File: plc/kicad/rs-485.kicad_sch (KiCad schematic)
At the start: 1 part, among them CN3 DB2ERC-5.08-4P

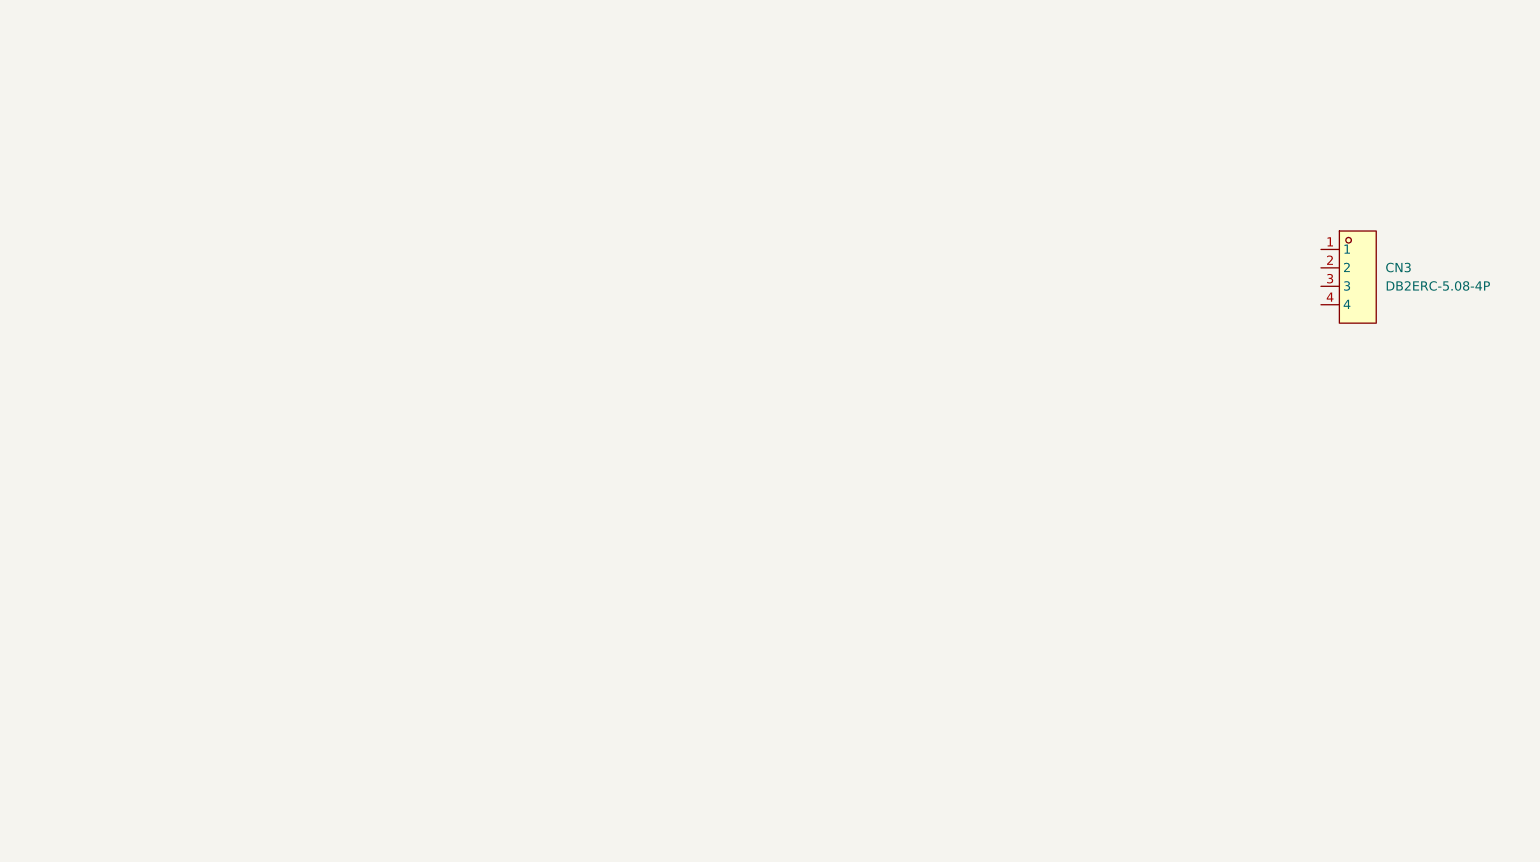
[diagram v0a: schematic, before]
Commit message: Added RS 485 circuit
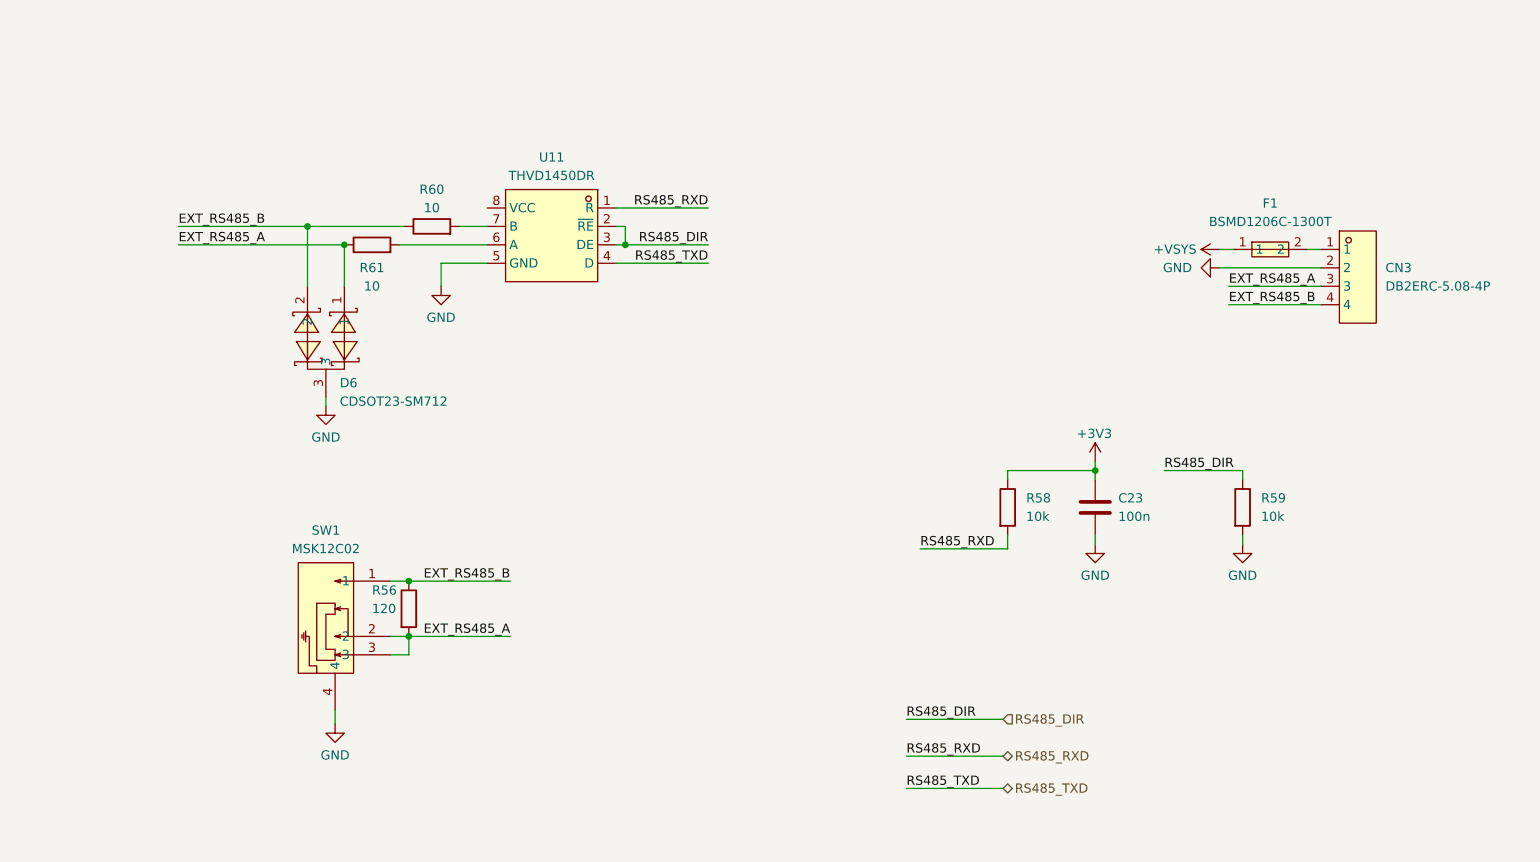
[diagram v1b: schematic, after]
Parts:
- added C23: 100n, Capacitor_SMD:C_0805_2012Metric, symbol Device:C
- added D6: CDSOT23-SM712, LibrePLC32:SOT-23_L2.9-W1.3-P1.90-LS2.4-BR, symbol LibrePLC32:CDSOT23-SM712
- added F1: BSMD1206C-1300T, LibrePLC32:F1206, symbol LibrePLC32:BSMD1206C-1300T
- added R56: 120, Resistor_SMD:R_0805_2012Metric, symbol Device:R
- added R58, R59: 10k, Resistor_SMD:R_0805_2012Metric, symbol Device:R
- added R60, R61: 10, Resistor_SMD:R_0805_2012Metric, symbol Device:R
- added SW1: MSK12C02, LibrePLC32:SW-TH_MSK12C02, symbol LibrePLC32:MSK12C02
- added U11: THVD1450DR, LibrePLC32:SOIC-8_L4.9-W3.9-P1.27-LS6.0-BL, symbol LibrePLC32:THVD1450DR
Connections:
- net at CN3.1: now also F1.2
- net GND: now reaches CN3.2
- net GND: now also C23.2, D6.3, R59.2, SW1.4, U11.5 (GND)
- net EXT_RS485_A: now reaches CN3.3
- net EXT_RS485_A: now also D6.1, R56.2, R61.1, SW1.2, SW1.3
- net EXT_RS485_B: now reaches CN3.4
- net EXT_RS485_B: now also D6.2, R56.1, R60.1, SW1.1
- new net: R60.2, U11.7 (B)
- new net: R61.2, U11.6 (A)
- new net +3V3: C23.1, R58.1
- new net +VSYS: F1.1
- new net RS485_DIR: R59.1, U11.2 (~{RE}), U11.3 (DE)
- new net RS485_RXD: R58.2, U11.1 (R)
- new net RS485_TXD: U11.4 (D)

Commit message: Added CAN circuit
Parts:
- removed F1: BSMD1206C-1300T, LibrePLC32:F1206, symbol LibrePLC32:BSMD1206C-1300T
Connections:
- net +VSYS: now also CN3.1
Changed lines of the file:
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@@
-	(wire
-		(pts
-			(xy 201.93 83.82) (xy 203.835 83.82)
-		)
-		(stroke
-			(width 0)
-			(type default)
-		)
-	)
 	(wire
 		(pts
@@
 	(wire
 		(pts
+			(xy 203.2 83.82) (xy 215.9 83.82)
+		)
+		(stroke
+			(width 0)
+			(type default)
+		)
+	)
+	(wire
+		(pts
 			(xy 203.2 91.44) (xy 215.9 91.44)
 		)
@@
 	(wire
 		(pts
-			(xy 201.93 86.36) (xy 215.9 86.36)
+			(xy 203.2 86.36) (xy 215.9 86.36)
 		)
 		(stroke
@@
 		(pts
 			(xy 58.42 80.645) (xy 76.2 80.645)
-		)
-		(stroke
-			(width 0)
-			(type default)
-		)
-	)
-	(wire
-		(pts
-			(xy 213.995 83.82) (xy 215.9 83.82)
 		)
 		(stroke
@@
 	)
 	(symbol
+		(lib_id "power:+VSW")
+		(at 203.2 83.82 90)
+		(unit 1)
+		(body_style 1)
+		(exclude_from_sim no)
+		(in_bom yes)
+		(on_board yes)
+		(in_pos_files yes)
+		(dnp no)
+		(fields_autoplaced yes)
+		(property "Reference" "#PWR0117"
+			(at 207.01 83.82 0)
+			(hide yes)
+			(show_name no)
+			(do_not_autoplace no)
+			(effects
+				(font
+					(size 1.27 1.27)
+				)
+			)
+		)
+		(property "Value" "+VSYS"
+			(at 200.025 83.8199 90)
+			(show_name no)
+			(do_not_autoplace no)
+			(effects
+				(font
+					(size 1.27 1.27)
+				)
+				(justify left)
+			)
+		)
+		(property "Footprint" ""
+			(at 203.2 83.82 0)
+			(hide yes)
+			(show_name no)
+			(do_not_autoplace no)
+			(effects
+				(font
+					(size 1.27 1.27)
+				)
+			)
+		)
+		(property "Datasheet" ""
+			(at 203.2 83.82 0)
+			(hide yes)
+			(show_name no)
+			(do_not_autoplace no)
+			(effects
+				(font
+					(size 1.27 1.27)
+				)
+			)
+		)
+		(property "Description" "Power symbol creates a global label with name \"+VSW\""
+			(at 203.2 83.82 0)
+			(hide yes)
+			(show_name no)
+			(do_not_autoplace no)
+			(effects
+				(font
+					(size 1.27 1.27)
+				)
+			)
+		)
+		(pin "1"
+		)
+		(instances
+			(project "LibrePLC32"
+				(path "/ef4c1a27-85a3-413a-9f93-a41c4f97eee5/58fa1ecb-ea1c-4a70-bb90-31ff9b441562"
+					(reference "#PWR0117")
+					(unit 1)
+				)
+			)
+		)
+	)
+	(symbol
 		(lib_id "LibrePLC32:DB2ERC-5.08-4P")
 		(at 219.71 87.63 0)
@@
 	)
 	(symbol
-		(lib_id "power:+VSW")
-		(at 201.93 83.82 90)
-		(unit 1)
-		(body_style 1)
-		(exclude_from_sim no)
-		(in_bom yes)
-		(on_board yes)
-		(in_pos_files yes)
-		(dnp no)
-		(fields_autoplaced yes)
-		(property "Reference" "#PWR0117"
-			(at 205.74 83.82 0)
-			(hide yes)
-			(show_name no)
-			(do_not_autoplace no)
-			(effects
-				(font
-					(size 1.27 1.27)
-				)
-			)
-		)
-		(property "Value" "+VSYS"
-			(at 198.755 83.8199 90)
-			(show_name no)
-			(do_not_autoplace no)
-			(effects
-				(font
-					(size 1.27 1.27)
-				)
-				(justify left)
-			)
-		)
-		(property "Footprint" ""
-			(at 201.93 83.82 0)
-			(hide yes)
-			(show_name no)
-			(do_not_autoplace no)
-			(effects
-				(font
-					(size 1.27 1.27)
-				)
-			)
-		)
-		(property "Datasheet" ""
-			(at 201.93 83.82 0)
-			(hide yes)
-			(show_name no)
-			(do_not_autoplace no)
-			(effects
-				(font
-					(size 1.27 1.27)
-				)
-			)
-		)
-		(property "Description" "Power symbol creates a global label with name \"+VSW\""
-			(at 201.93 83.82 0)
-			(hide yes)
-			(show_name no)
-			(do_not_autoplace no)
-			(effects
-				(font
-					(size 1.27 1.27)
-				)
-			)
-		)
-		(pin "1"
-		)
-		(instances
-			(project "LibrePLC32"
-				(path "/ef4c1a27-85a3-413a-9f93-a41c4f97eee5/58fa1ecb-ea1c-4a70-bb90-31ff9b441562"
-					(reference "#PWR0117")
-					(unit 1)
-				)
-			)
-		)
-	)
-	(symbol
 		(lib_id "LibrePLC32:THVD1450DR")
 		(at 109.855 81.915 0)
@@
 	(symbol
 		(lib_id "power:GND")
-		(at 201.93 86.36 270)
+		(at 203.2 86.36 270)
 		(unit 1)
 		(body_style 1)
@@
 		(fields_autoplaced yes)
 		(property "Reference" "#PWR0126"
-			(at 195.58 86.36 0)
+			(at 196.85 86.36 0)
 			(hide yes)
 			(show_name no)
@@
 		)
 		(property "Value" "GND"
-			(at 198.12 86.3599 90)
+			(at 199.39 86.3599 90)
 			(show_name no)
 			(do_not_autoplace no)
@@
 		)
 		(property "Footprint" ""
-			(at 201.93 86.36 0)
+			(at 203.2 86.36 0)
 			(hide yes)
 			(show_name no)
@@
 		)
 		(property "Datasheet" ""
-			(at 201.93 86.36 0)
+			(at 203.2 86.36 0)
 			(hide yes)
 			(show_name no)
@@
 		)
 		(property "Description" "Power symbol creates a global label with name \"GND\" , ground"
-			(at 201.93 86.36 0)
+			(at 203.2 86.36 0)
 			(hide yes)
 			(show_name no)
@@
 					(unit 1)
 				)
-			)
-		)
-	)
-	(symbol
-		(lib_id "LibrePLC32:BSMD1206C-1300T")
-		(at 208.915 83.82 0)
-		(unit 1)
-		(body_style 1)
-		(exclude_from_sim no)
-		(in_bom yes)
-		(on_board yes)
-		(in_pos_files yes)
-		(dnp no)
-		(fields_autoplaced yes)
-		(property "Reference" "F1"
-			(at 208.915 77.47 0)
-			(show_name no)
-			(do_not_autoplace no)
-			(effects
-				(font
-					(size 1.27 1.27)
-				)
-			)
-		)
-		(property "Value" "BSMD1206C-1300T"
-			(at 208.915 80.01 0)
-			(show_name no)
-			(do_not_autoplace no)
-			(effects
-				(font
-					(size 1.27 1.27)
-				)
-			)
-		)
-		(property "Footprint" "LibrePLC32:F1206"
-			(at 208.915 91.44 0)
-			(hide yes)
-			(show_name no)
-			(do_not_autoplace no)
-			(effects
-				(font
-					(size 1.27 1.27)
-				)
-			)
-		)
-		(property "Datasheet" "https://www.lcsc.com/datasheet/C41367225.pdf"
-			(at 208.915 93.98 0)
-			(hide yes)
-			(show_name no)
-			(do_not_autoplace no)
-			(effects
-				(font
-					(size 1.27 1.27)
-				)
-			)
-		)
-		(property "Description" ""
-			(at 208.915 83.82 0)
-			(hide yes)
-			(show_name no)
-			(do_not_autoplace no)
-			(effects
-				(font
-					(size 1.27 1.27)
-				)
-			)
-		)
-		(property "Manufacturer" "BHFUSE(佰宏)"
-			(at 208.915 96.52 0)
-			(hide yes)
-			(show_name no)
-			(do_not_autoplace no)
-			(effects
-				(font
-					(size 1.27 1.27)
-				)
-			)
-		)
-		(property "MPN" "BSMD1206C-1300T"
-			(at 208.915 99.06 0)
-			(hide yes)
-			(show_name no)
-			(do_not_autoplace no)
-			(effects
-				(font
-					(size 1.27 1.27)
-				)
-			)
-		)
-		(property "LCSC Part" "C41367225"
-			(at 208.915 101.6 0)
-			(hide yes)
-			(show_name no)
-			(do_not_autoplace no)
-			(effects
-				(font
-					(size 1.27 1.27)
-				)
-			)
-		)
-		(pin "1"
-		)
-		(pin "2"
-		)
-		(instances
-			(project "LibrePLC32"
-				(path "/ef4c1a27-85a3-413a-9f93-a41c4f97eee5/58fa1ecb-ea1c-4a70-bb90-31ff9b441562"
-					(reference "F1")
-					(unit 1)
-				)

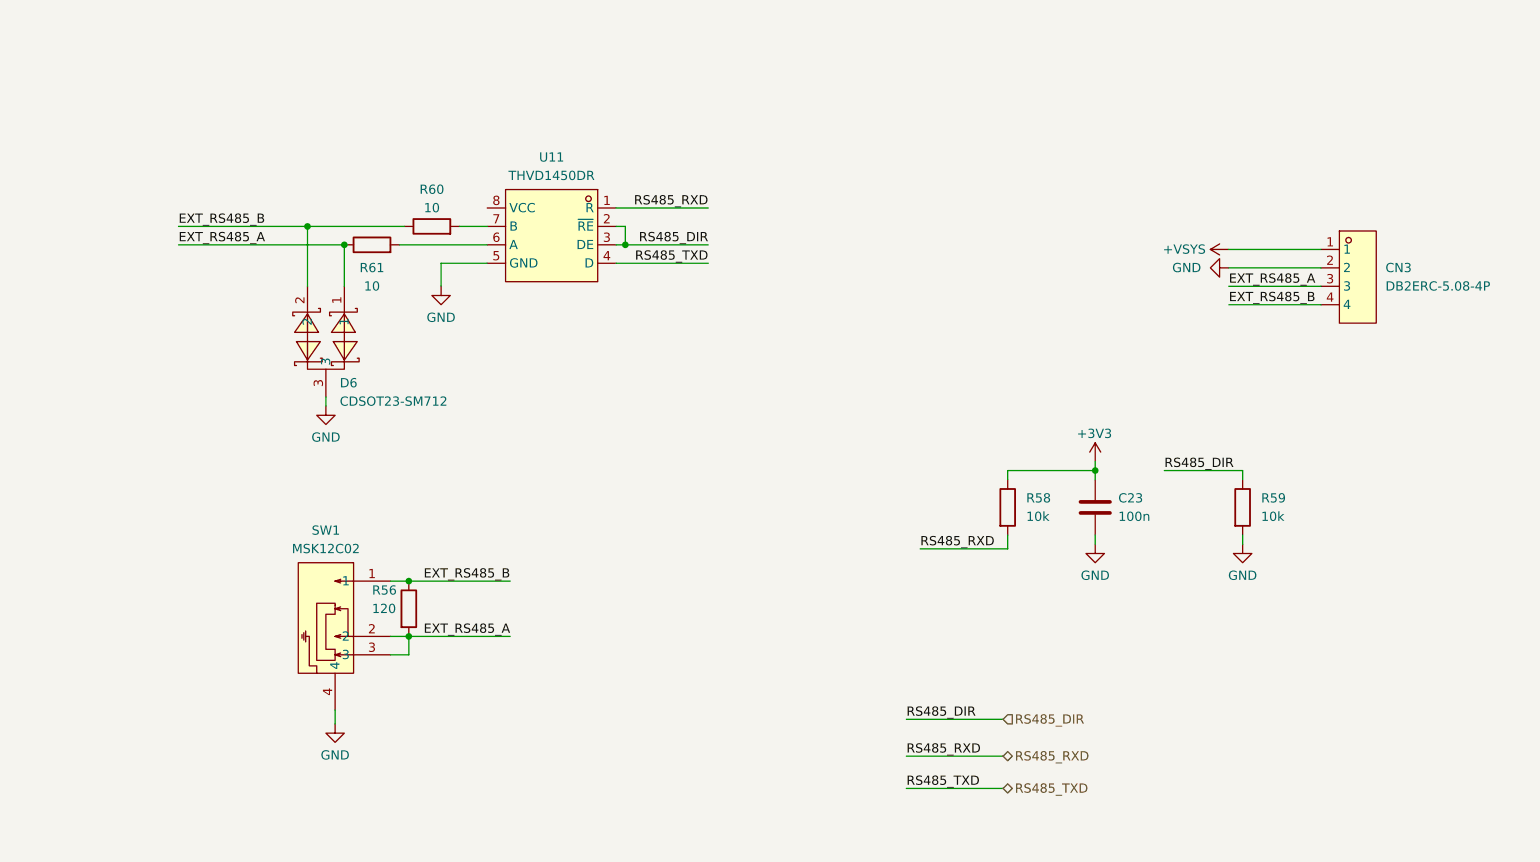
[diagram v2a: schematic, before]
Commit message: Added netclasses
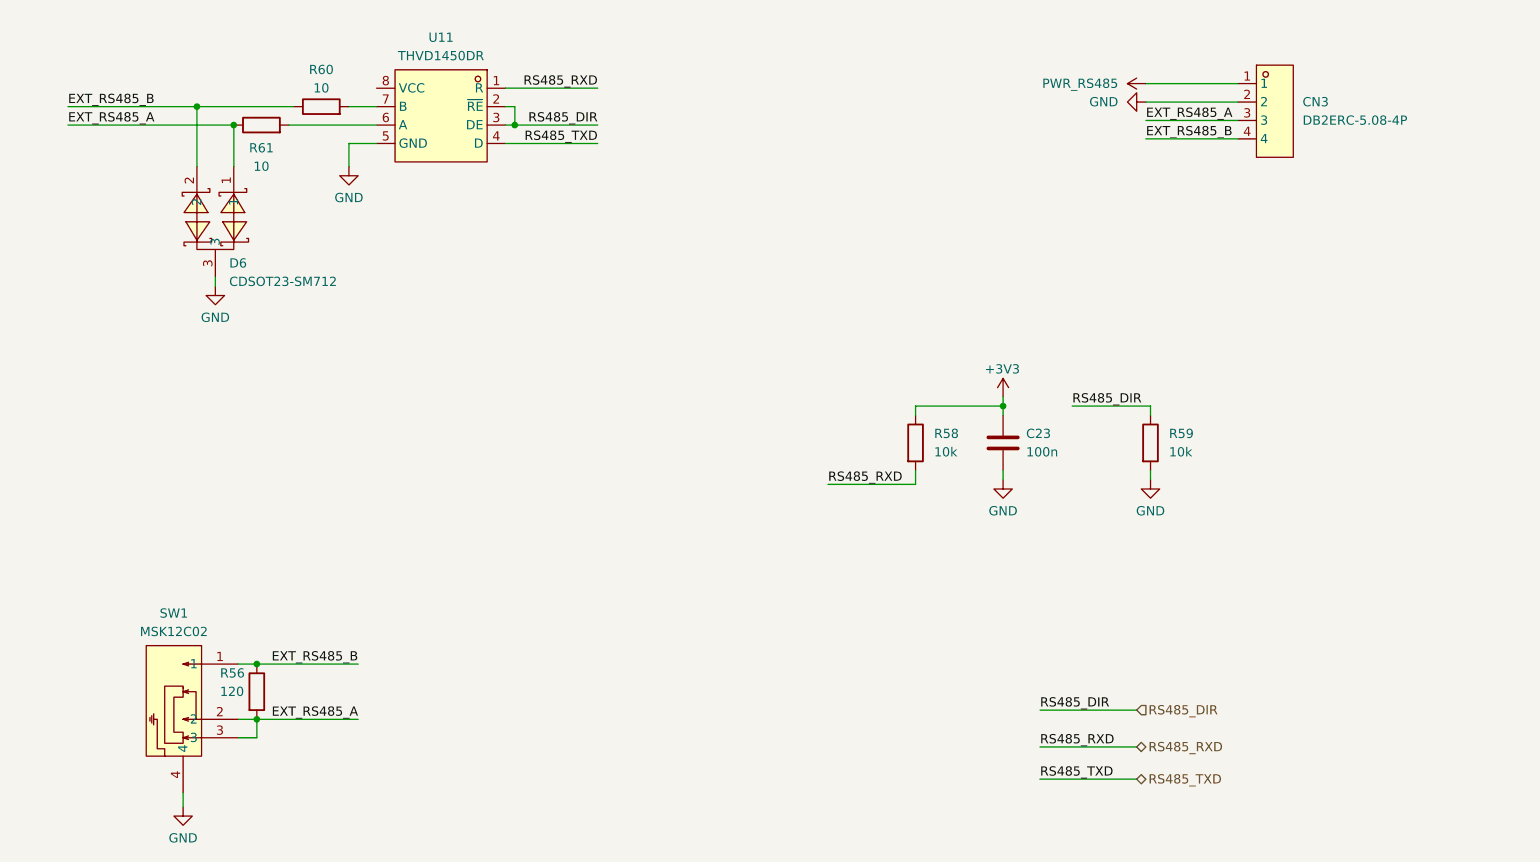
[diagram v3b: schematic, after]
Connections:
- net +VSYS renamed PWR_RS485
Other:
- moved on the sheet: C23, CN3, D6, R56, R58, R59, R60, R61, SW1, U11
